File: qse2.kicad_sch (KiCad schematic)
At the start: 81 parts, among them J1 5-1814832-1, J2 5-1814832-1, J3 Conn_02x08_Odd_Even, J4 SJ-3524-SMT, J6 Conn_01x02, J7 B4B-XH-A_LF__SN_, U1 SN74LVC1G14DBV, U10 SN74LVC1G14DBV, U11 NCP114ASN330T1G, U2 SN74LVC1G14DBV, U3 SN74CBT3253, U4 SN74AC74PW, U5 AD8137ARZ-R7, U6 NCV8114ASN165T1G, U7 UA78M05IDCYR, U8 AP2120N-2.5TRG1, U9 AD8137ARZ-R7

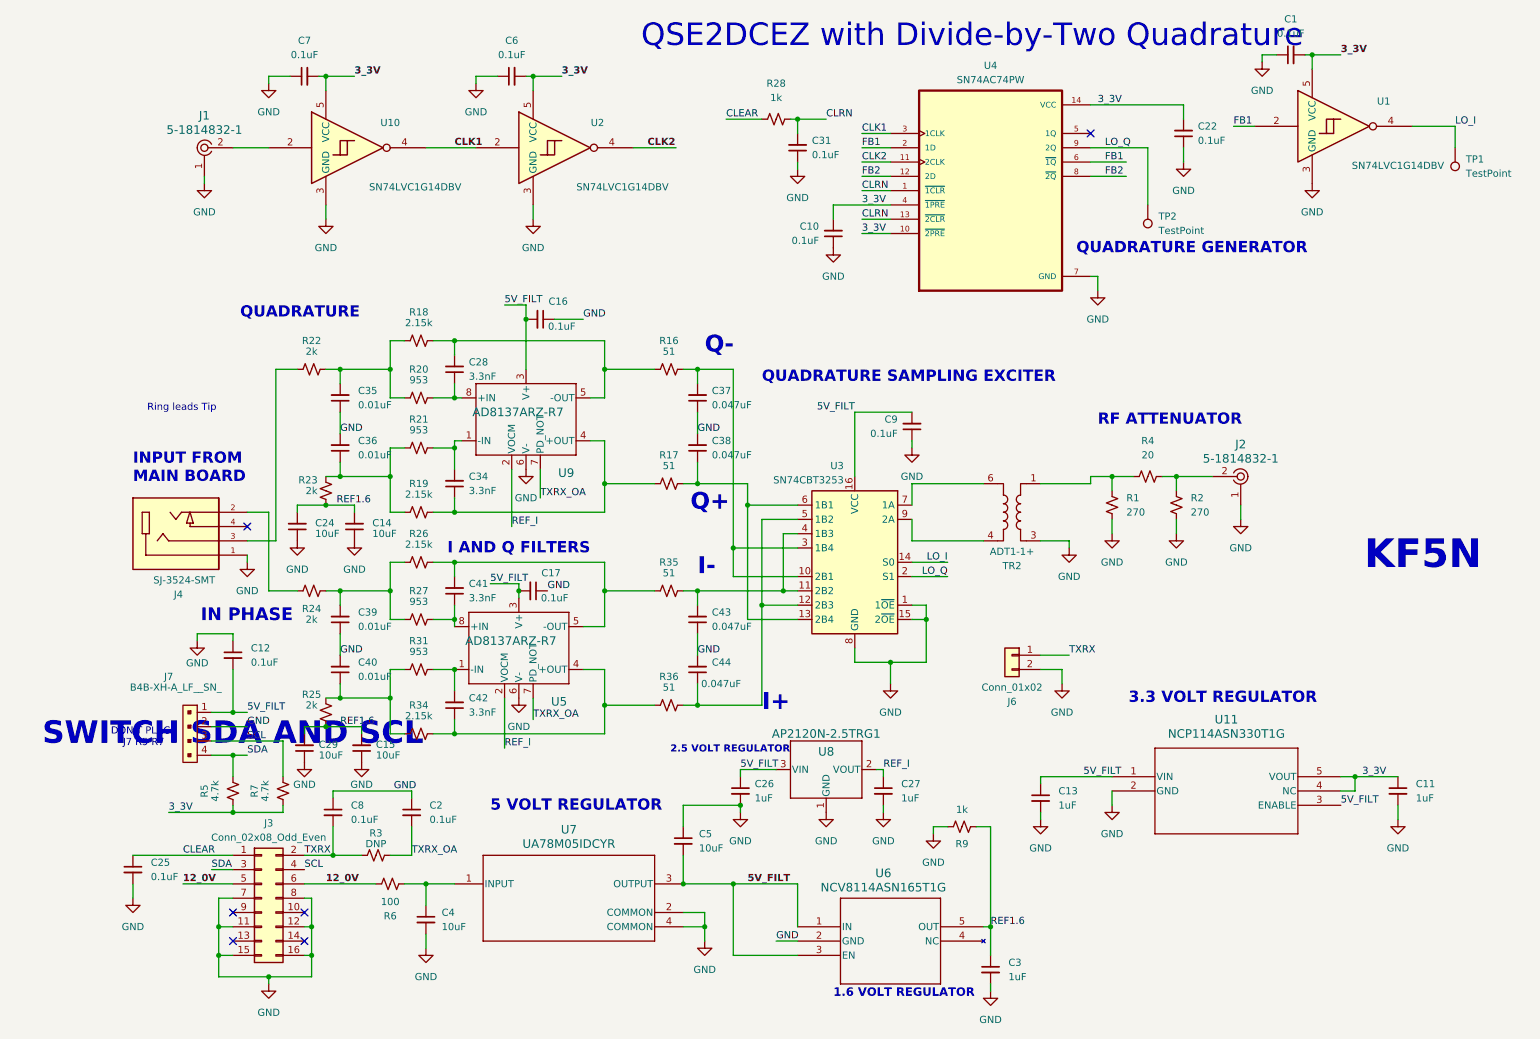
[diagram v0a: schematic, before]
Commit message: Updated to new Kicad.
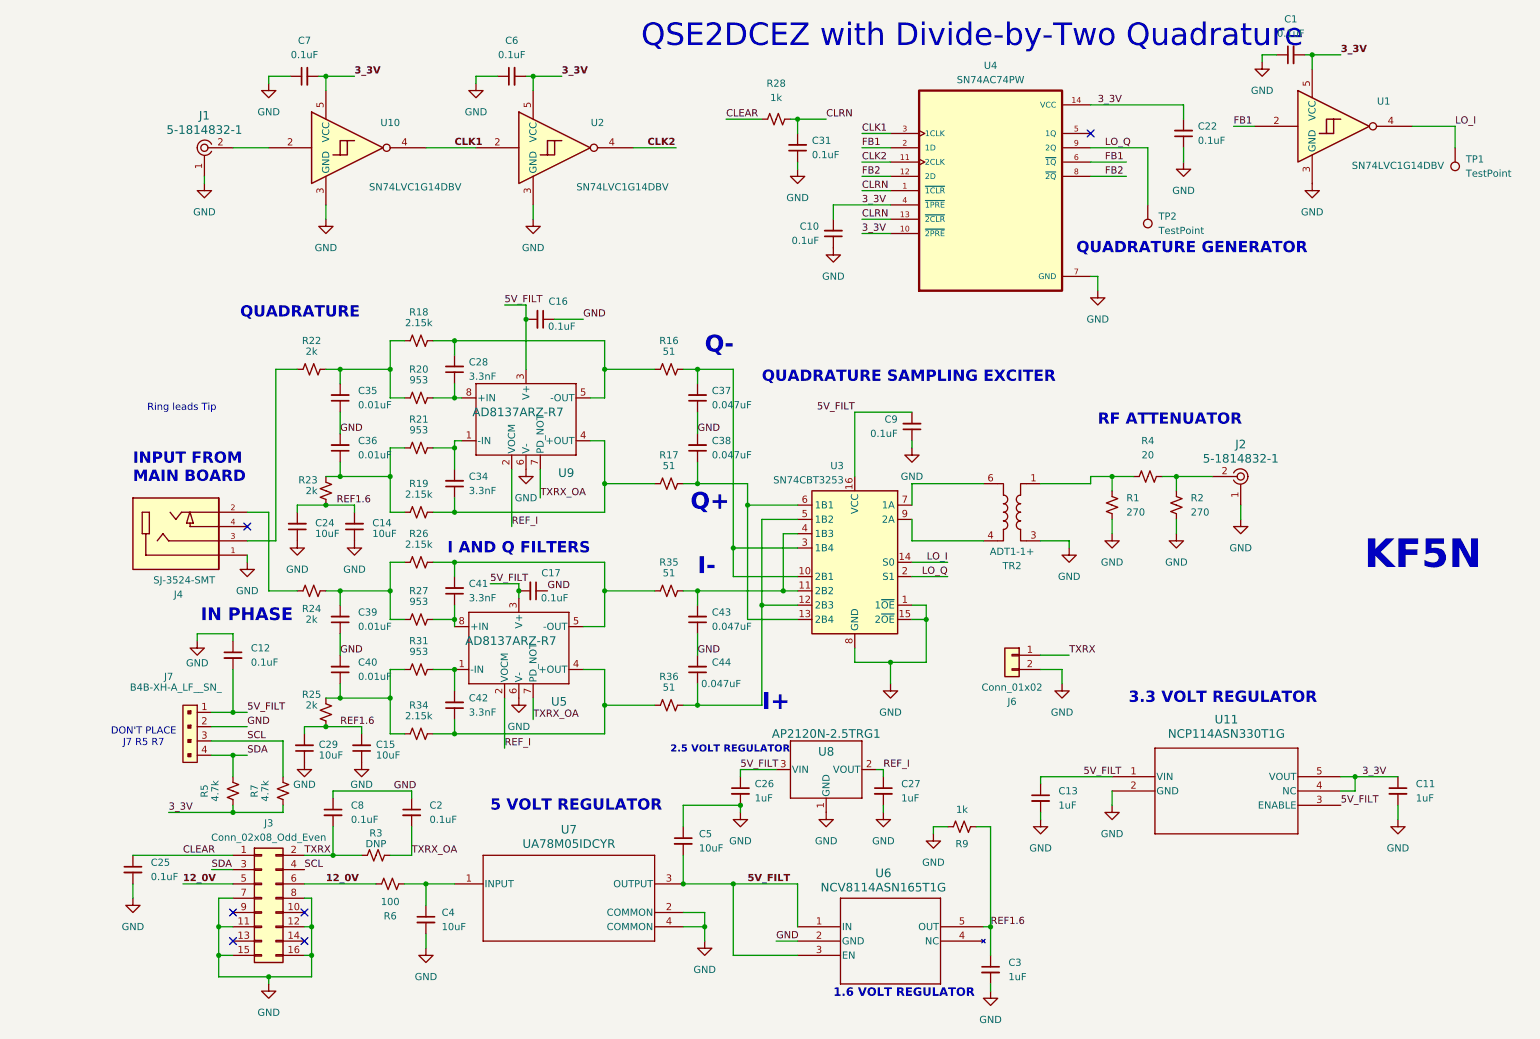
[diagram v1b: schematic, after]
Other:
- note removed: "SWITCH SDA AND SCL"

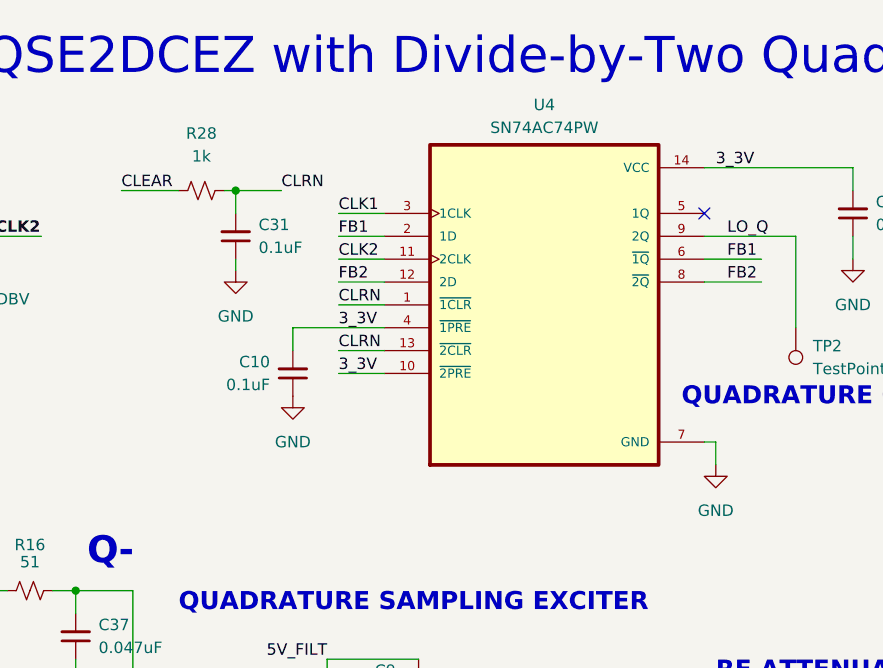
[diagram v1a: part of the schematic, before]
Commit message: Fixed flip-flop part number.
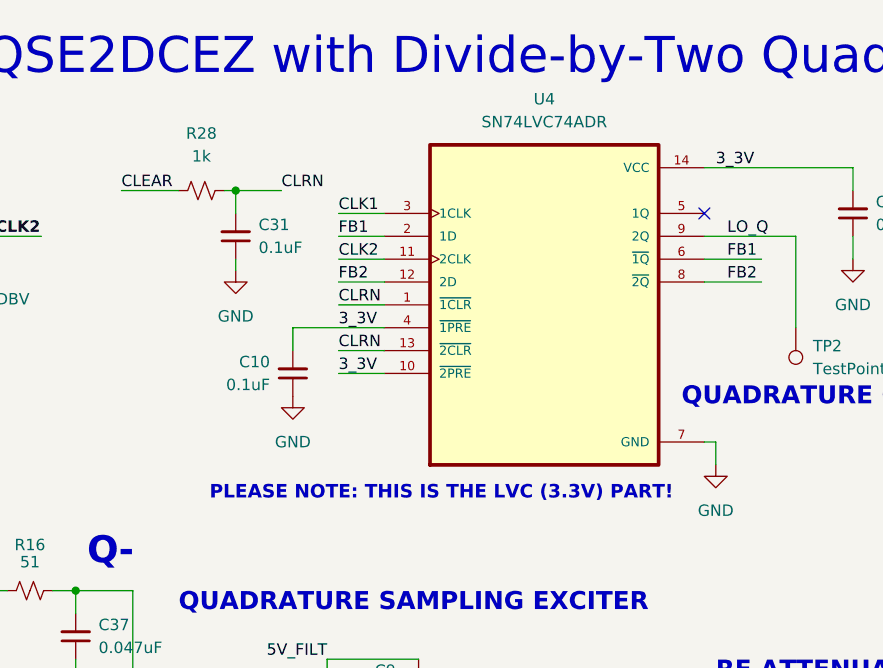
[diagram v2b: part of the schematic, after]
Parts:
- U4: value SN74AC74PW -> SN74LVC74ADR
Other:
- note added: "PLEASE NOTE: THIS IS THE LVC (3.3V) PART!"
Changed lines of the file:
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@@
 		)
 	)
+	(text "PLEASE NOTE: THIS IS THE LVC (3.3V) PART!"
+		(exclude_from_sim no)
+		(at 157.48 67.945 0)
+		(effects
+			(font
+				(size 1.5 1.5)
+				(thickness 0.3)
+				(bold yes)
+			)
+		)
+	)
 	(text "INPUT FROM\nMAIN BOARD"
 		(exclude_from_sim no)
@@
 		(fields_autoplaced yes)
 		(property "Reference" "U4"
-			(at 168.91 24.765 0)
+			(at 168.91 24.13 0)
 			(show_name no)
 			(do_not_autoplace no)
@@
 			)
 		)
-		(property "Value" "SN74AC74PW"
-			(at 168.91 27.305 0)
+		(property "Value" "SN74LVC74ADR"
+			(at 168.91 26.67 0)
 			(show_name no)
 			(do_not_autoplace no)
